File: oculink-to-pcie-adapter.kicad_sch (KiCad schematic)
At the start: 7 parts, among them J4 Molex_Mini-Fit-Jr_2x4_0455860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, J5 Molex_Mini-Fit_2x4_172448-000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

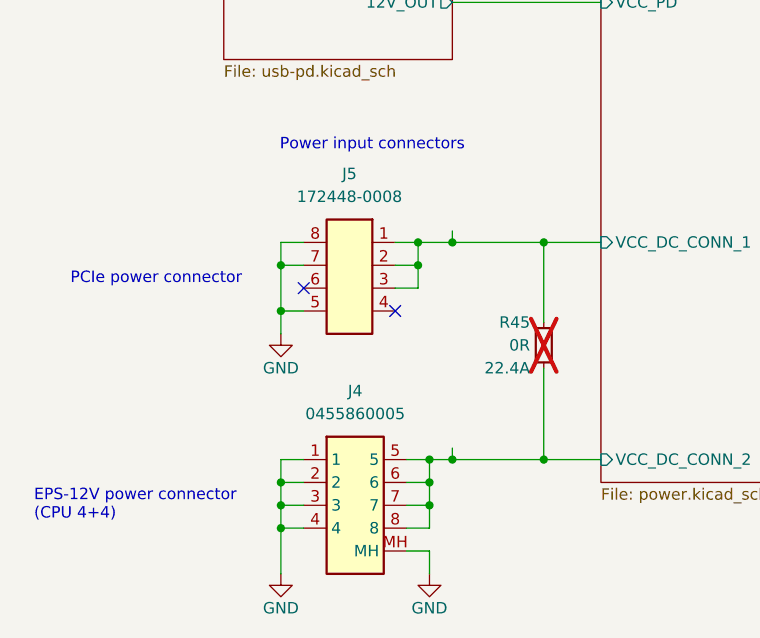
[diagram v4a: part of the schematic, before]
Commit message: [#79262] Adjusted placement
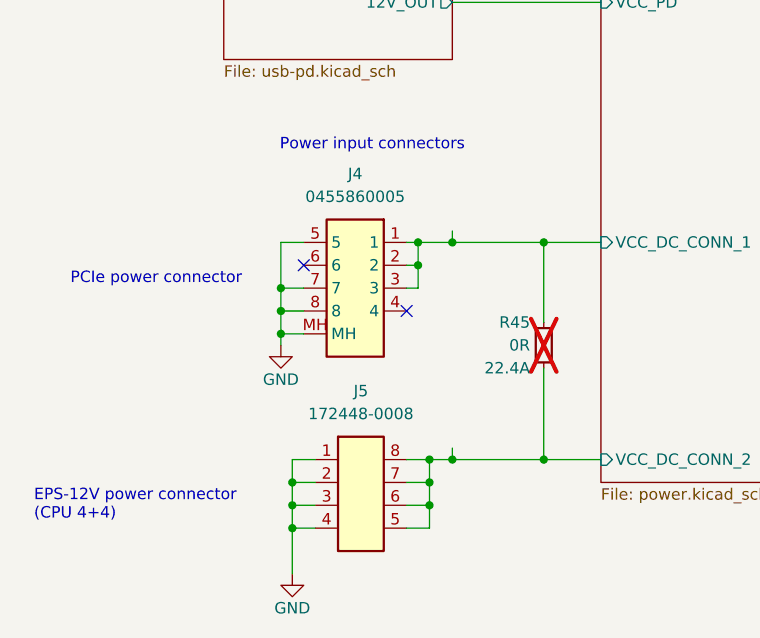
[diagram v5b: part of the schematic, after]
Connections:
- net GND: now also J4.5, J4.7, J4.8, J5.1, J5.2, J5.3, J5.4; no longer J4.1, J4.2, J4.3, J4.4, J5.5, J5.7, J5.8
- net Power/VCC_DC_CONN_1: now also J4.1, J4.2, J4.3; no longer J5.1, J5.2, J5.3
- net Power/VCC_DC_CONN_2: now also J5.5, J5.6, J5.7, J5.8; no longer J4.5, J4.6, J4.7, J4.8
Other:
- moved on the sheet: J4, J5

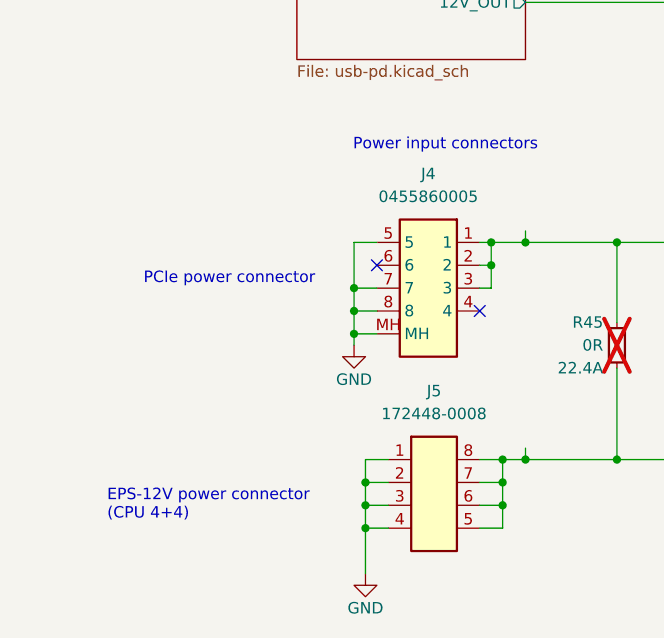
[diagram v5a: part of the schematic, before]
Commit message: [#79790] Made board smaller, moved connectors to shorter edge
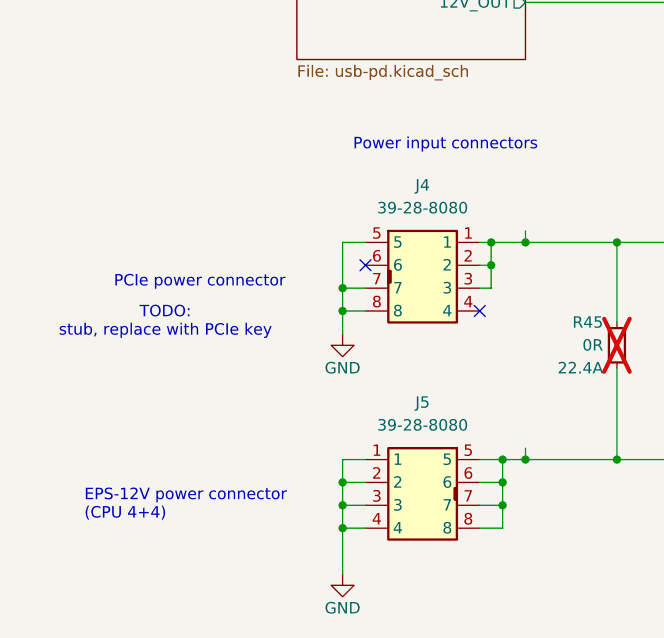
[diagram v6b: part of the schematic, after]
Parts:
- removed J4: Molex_Mini-Fit-Jr_2x4_0455860005, antmicro-footprints:Molex_Mini-Fit-Jr_2x4_0455860005, symbol antmicroWire2BoardConnectors:Molex_Mini-Fit-Jr_2x4_0455860005
- removed J5: Molex_Mini-Fit_2x4_172448-0008_Horizontal, antmicro-footprints:Molex_Mini-Fit_2x4_172448-0008_Horizontal, symbol antmicroWire2BoardConnectors:Molex_Mini-Fit_2x4_172448-0008_Horizontal
- added J4, J5: Molex_Mini-Fit-Jr_2x4_39-28-8080, antmicro-footprints:MOLEX_39288080, symbol antmicroWire2BoardConnectors:Molex_Mini-Fit-Jr_2x4_39-28-8080
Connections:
- net GND: now also J4.5, J4.7, J4.8, J5.1, J5.2, J5.3, J5.4
- net Power/VCC_DC_CONN_1: now also J4.1, J4.2, J4.3
- net Power/VCC_DC_CONN_2: now also J5.5, J5.6, J5.7, J5.8
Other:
- note added: "TODO: stub, replace with PCIe key"

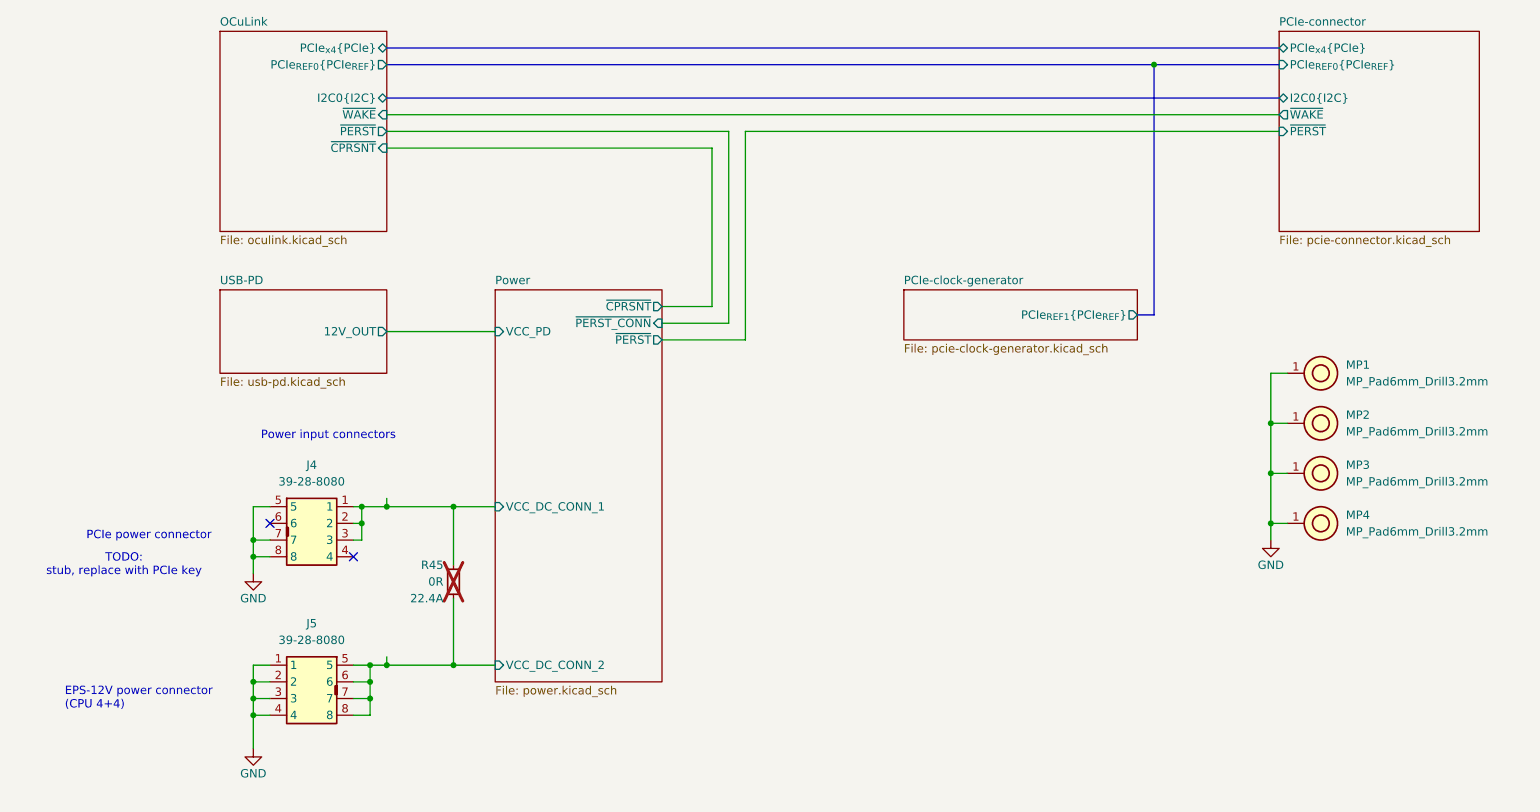
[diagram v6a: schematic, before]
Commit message: [#79790] Finalized rerouting
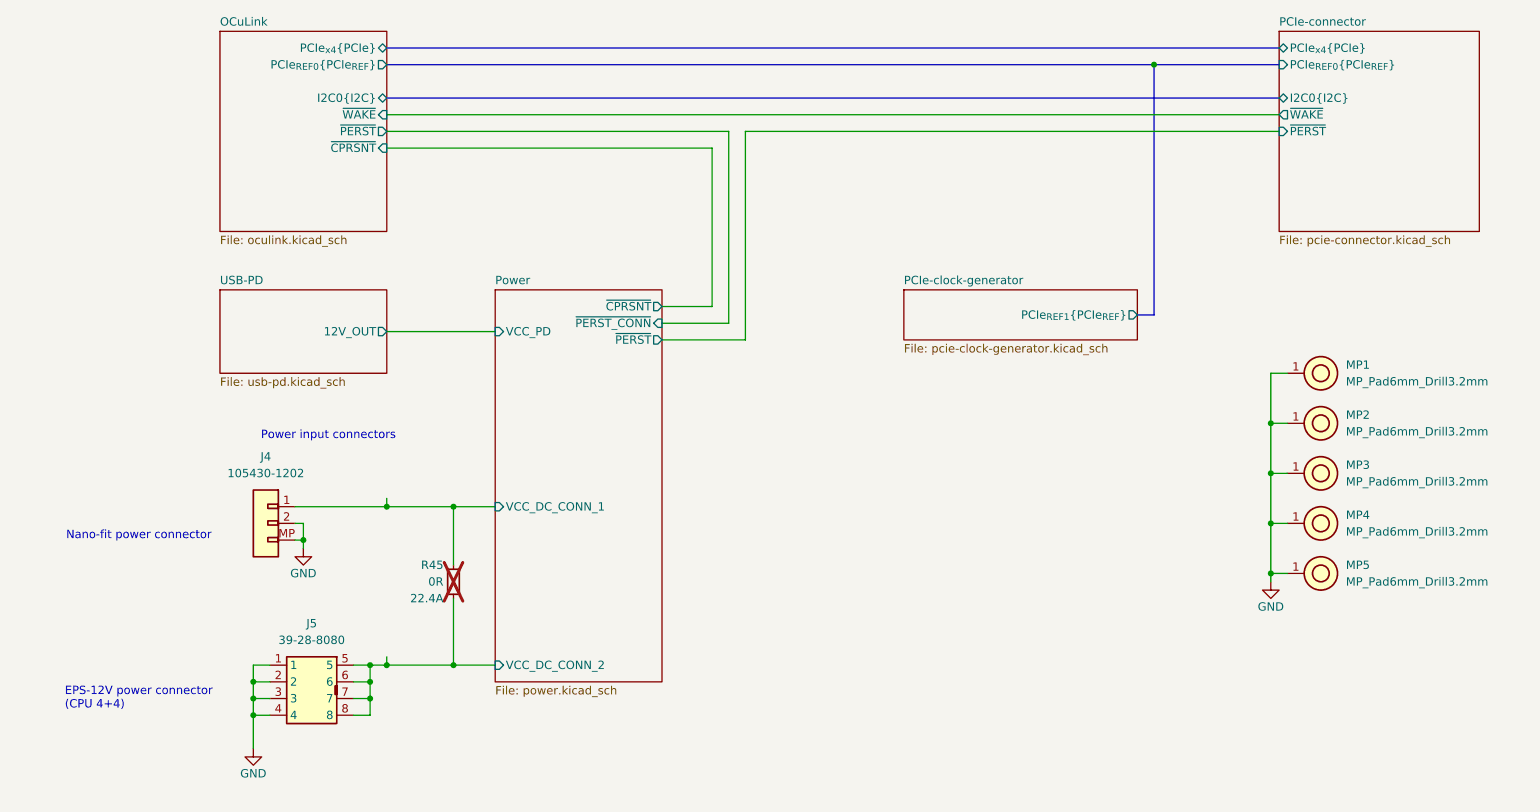
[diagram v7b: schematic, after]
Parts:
- removed J4: Molex_Mini-Fit-Jr_2x4_39-28-8080, antmicro-footprints:MOLEX_39288080, symbol antmicroWire2BoardConnectors:Molex_Mini-Fit-Jr_2x4_39-28-8080
- added J4: Molex_Nano-Fit_1x2_SMD_1054301202, antmicro-footprints:Conn_Molex_Nano-Fit_1x2_SMD_1054301202, symbol antmicroWire2BoardConnectors:Molex_Nano-Fit_1x2_SMD_1054301202
- added MP5: MP_Pad6mm_Drill3.2mm, antmicro-footprints:MP_Pad6mm_Drill3.2mm, symbol antmicroMechanicalParts:MP_Pad6mm_Drill3.2mm
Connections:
- net GND: now also J4.2, J4.MP, MP5.1
- net Power/VCC_DC_CONN_1: now also J4.1
- no-connect marks 2 -> 0
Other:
- note added: "Nano-fit power connector"
- note removed: "PCIe power connector"
- note removed: "TODO: stub, replace with PCIe key"
